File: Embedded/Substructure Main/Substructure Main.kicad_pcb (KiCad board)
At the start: 2 copper layers, 60 parts, among them J1 MicroSD, J2 C Pins, J3 Coin Cell, U1 G0 FFC, U10 LD1117S50TR_SOT223, U2 G1 FFC, U3 S FFC, U4 USB2513B_Bi, U5 MCP7940N-xMNY, U6 INA220AIDGSR, U7 M FFC, U8 F FFC, U9 LD1117S33TR_SOT223, Y1 TSX-3225 24MF18X-C0, Y2 CM7V-T1A

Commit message: Begun Component Layout
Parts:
- U7: moved to B.Cu
- moved U1 98.5 mm to (106.0, 84.2), turned to -90 degrees
- moved U2 96.5 mm to (144.7, 83.0), turned to 90 degrees
- moved U3 93.8 mm to (144.8, 93.2), turned to 90 degrees
- moved C12 93.1 mm to (137.5, 131.7)
- moved C15 93.1 mm to (137.5, 129.0)
- moved C10 93.1 mm to (142.7, 137.0)
- moved C11 93.1 mm to (142.7, 138.0)
- moved C13 93.1 mm to (140.5, 136.0)
- moved C16 93.1 mm to (143.5, 136.0)
- moved C22 93.1 mm to (147.0, 132.2)
- moved C4 93.1 mm to (138.2, 124.4)
- moved C5 93.1 mm to (144.9, 124.4)
- moved C6 93.1 mm to (137.5, 126.0)
- moved C7 93.1 mm to (147.0, 131.2)
- moved C8 93.1 mm to (137.5, 127.0)
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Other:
- board outline added: 50 x 40 mm

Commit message: Added Sensored V2 Board
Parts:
- U11: value ~ -> Sensored; footprint Sensored:Sensored -> Custom Modules:Sensored
- moved U11 28.0 mm to (93.4, 139.8)
- renumbered C26 to C1, C3 to C10, C4 to C11, C5 to C12, C6 to C13, C7 to C14, C8 to C15, C9 to C16, C10 to C17, C11 to C18, C12 to C19, C28 to C2, C13 to C20, C14 to C21, C15 to C22, C16 to C23, C22 to C24, C17 to C25, C18 to C26, C19 to C27, C20 to C28, C21 to C29, C27 to C3, C29 to C4, C25 to C5, C1 to C6, C23 to C7, C2 to C8, C24 to C9, J2 to J1, J1 to J2, R3 to R1, R4 to R2, R1 to R3, R2 to R4, U6 to U10, U8 to U2, U7 to U4, U2 to U5, U9 to U6, U10 to U7, U4 to U8, U5 to U9

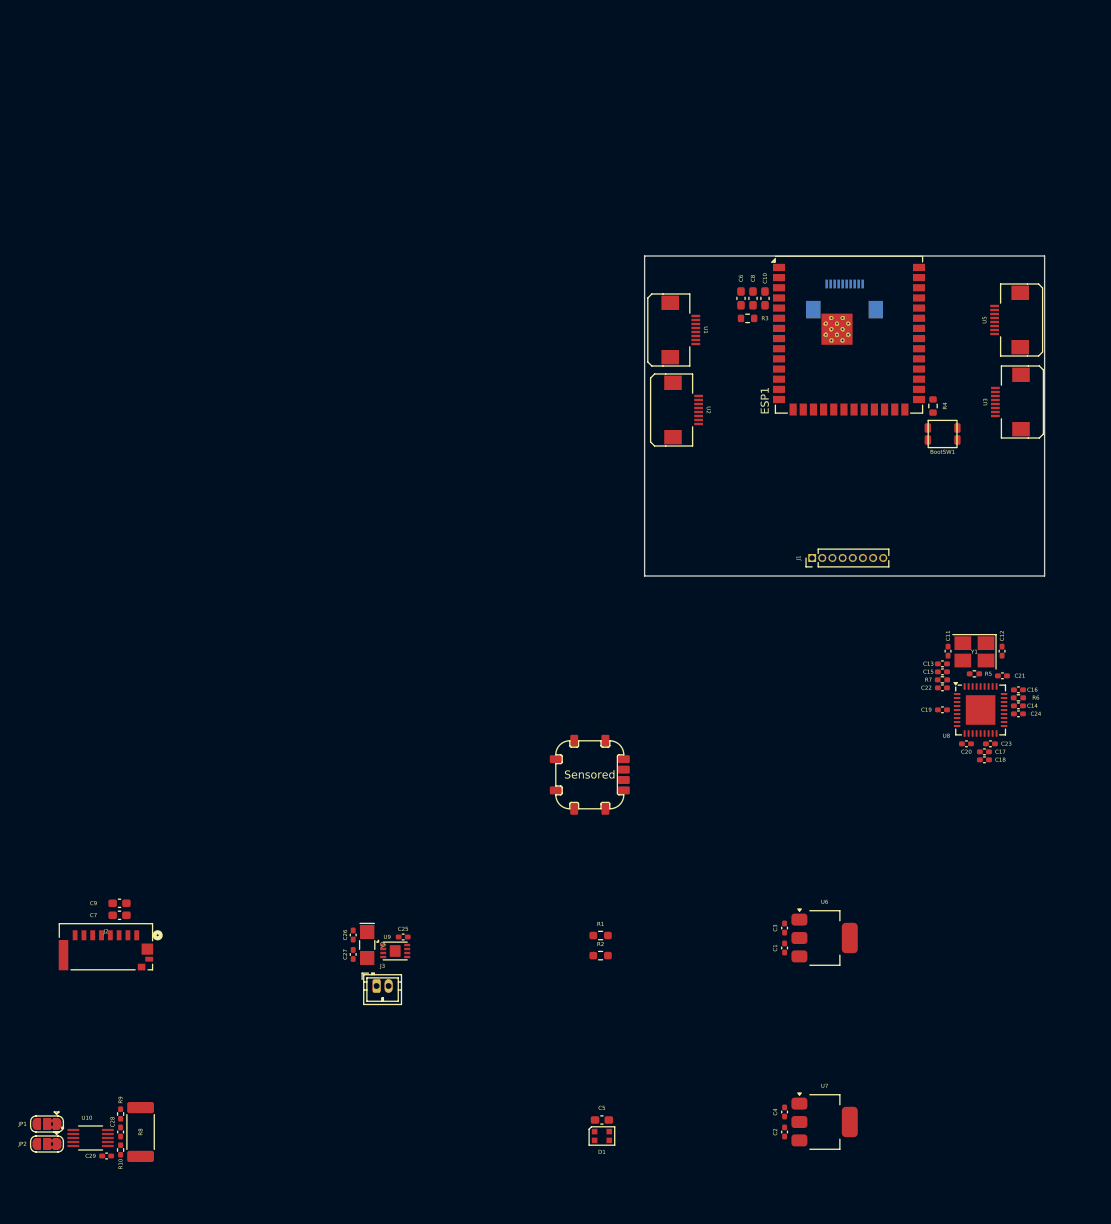
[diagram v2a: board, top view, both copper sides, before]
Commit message: Added Component placement & edge cuts
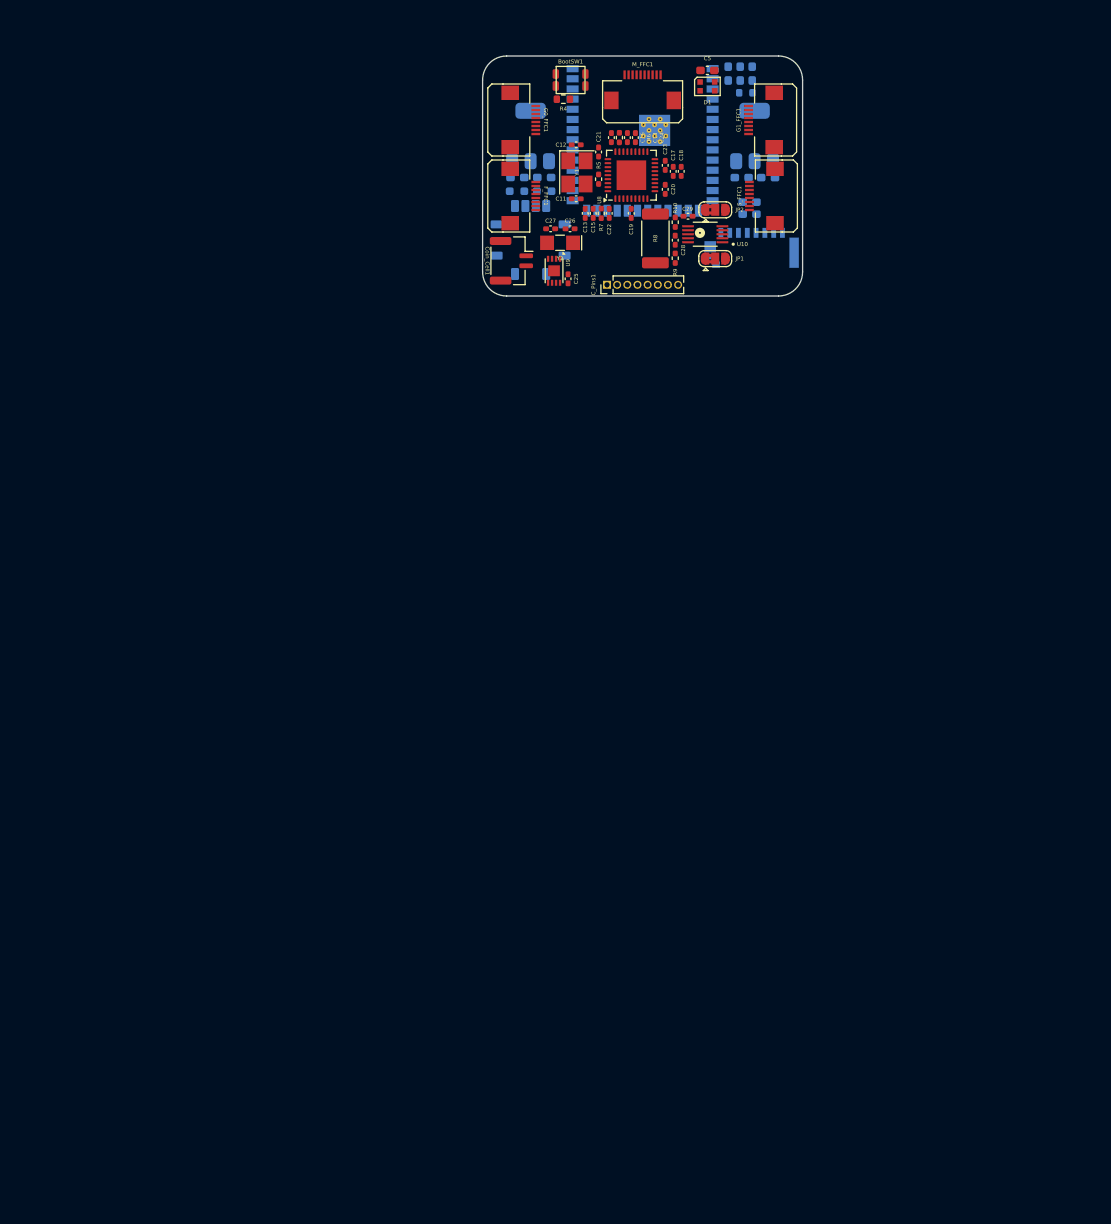
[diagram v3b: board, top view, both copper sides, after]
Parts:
- C1, C2, C3, C4: footprint Capacitor_SMD:C_0402_1005Metric_Pad0.74x0.62mm_HandSolder -> Capacitor_SMD:C_0603_1608Metric_Pad1.08x0.95mm_HandSolder; moved to B.Cu
- C10, C6, C7, C8, C9, ESP1, J2, R1, R2, R3, U11, U6, U7: moved to B.Cu
- Coin_Cell1: renamed from J3; footprint Connector_JST:JST_ZH_B2B-ZR_1x02_P1.50mm_Vertical -> Connector_JST:JST_GH_SM02B-GHS-TB_1x02-1MP_P1.25mm_Horizontal
- M_FFC1: renamed from U4; moved to F.Cu
- moved JP2 143.6 mm to (109.1, 69.2), turned to 0 degrees
- moved C29 138.1 mm to (105.7, 70.0), turned to 0 degrees
- moved JP1 136.7 mm to (109.1, 75.3), turned to 0 degrees
- moved U10 136.6 mm to (107.8, 72.3), turned to 180 degrees
- moved R10 135.1 mm to (104.1, 70.8), turned to -90 degrees
- moved C5 131.9 mm to (108.1, 51.8)
- moved D1 131.9 mm to (108.1, 53.8)
- moved C28 131.3 mm to (104.1, 73.0), turned to 90 degrees
- moved R8 128.9 mm to (101.6, 72.8), turned to 90 degrees
- moved U7 128.6 mm to (86.0, 60.0), turned to 90 degrees
- moved R9 127.5 mm to (104.1, 75.3), turned to 90 degrees
- moved C2 123.9 mm to (84.3, 65.2), turned to 0 degrees
- moved C4 120.6 mm to (87.7, 65.2), turned to 0 degrees
- moved J2 119.3 mm to (113.6, 72.1), turned to 180 degrees
- moved C7 119.0 mm to (113.4, 68.3)
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- renumbered J1 to C_Pins1, U2 to F_FFC1, U1 to G0_FFC1, U5 to G1_FFC1, U3 to S_FFC1
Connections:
- Coin_Cell1 pad 1: Net-(J3-Pin_1) -> GND
- Coin_Cell1 pad 2: GND -> Net-(Coin_Cell1-Pin_2)
- U9 pad 3: Net-(J3-Pin_1) -> Net-(Coin_Cell1-Pin_2)
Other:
- board size 50 x 40 mm -> 40 x 30 mm

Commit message: Modified Files (Synchronisation Update)
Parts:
- moved C5 3.20 mm to (108.0, 55.0)
- moved C6 3.10 mm to (110.6, 52.1)
- moved R3 1.50 mm to (111.4, 54.5), turned to 180 degrees
- moved C10 1.40 mm to (112.1, 52.1)
- moved C8 1.40 mm to (113.6, 52.1)
- moved D1 0.81 mm to (108.0, 53.0)
- moved ESP1 0.09 mm to (100.0, 59.9)
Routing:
- net +3V3: track 0.00 -> 13.0 mm
- net Net-(U8-XTALOUT): track 0.00 -> 8.09 mm
- net Net-(U8-XTALIN/CLKIN): track 0.00 -> 5.14 mm
- net Net-(ESP1-GPIO0/BOOT): track 0.00 -> 3.96 mm
- net Net-(ESP1-EN): track 0.00 -> 3.61 mm
- net Net-(U8-CRFILT): track 0.00 -> 3.33 mm
- net I2C SDA: track 0.00 -> 1.91 mm
- net I2C SCL: track 0.00 -> 1.91 mm
- added copper zone on F.Cu, net +3V3
- added copper zone on B.Cu, net GND

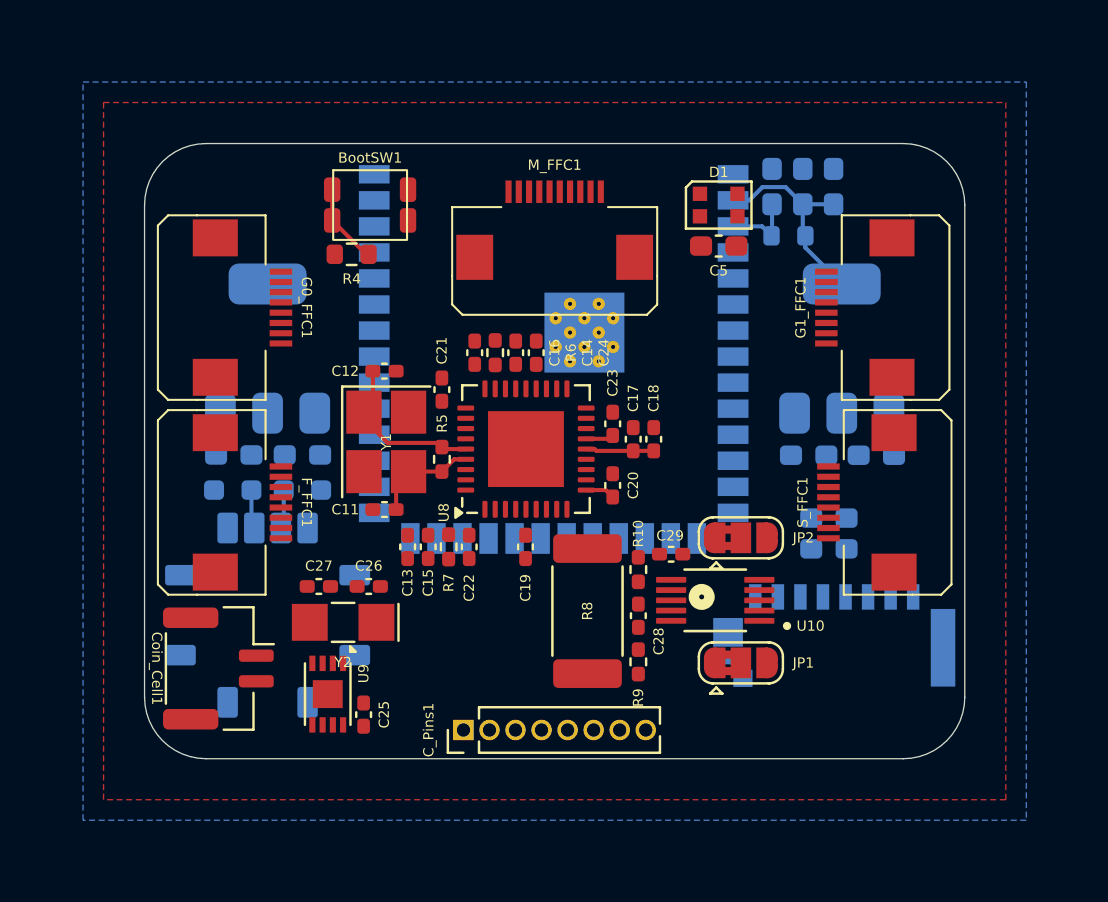
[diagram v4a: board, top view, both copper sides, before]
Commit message: Modified Board from 2 Layer to 4 Layers & Routed close components
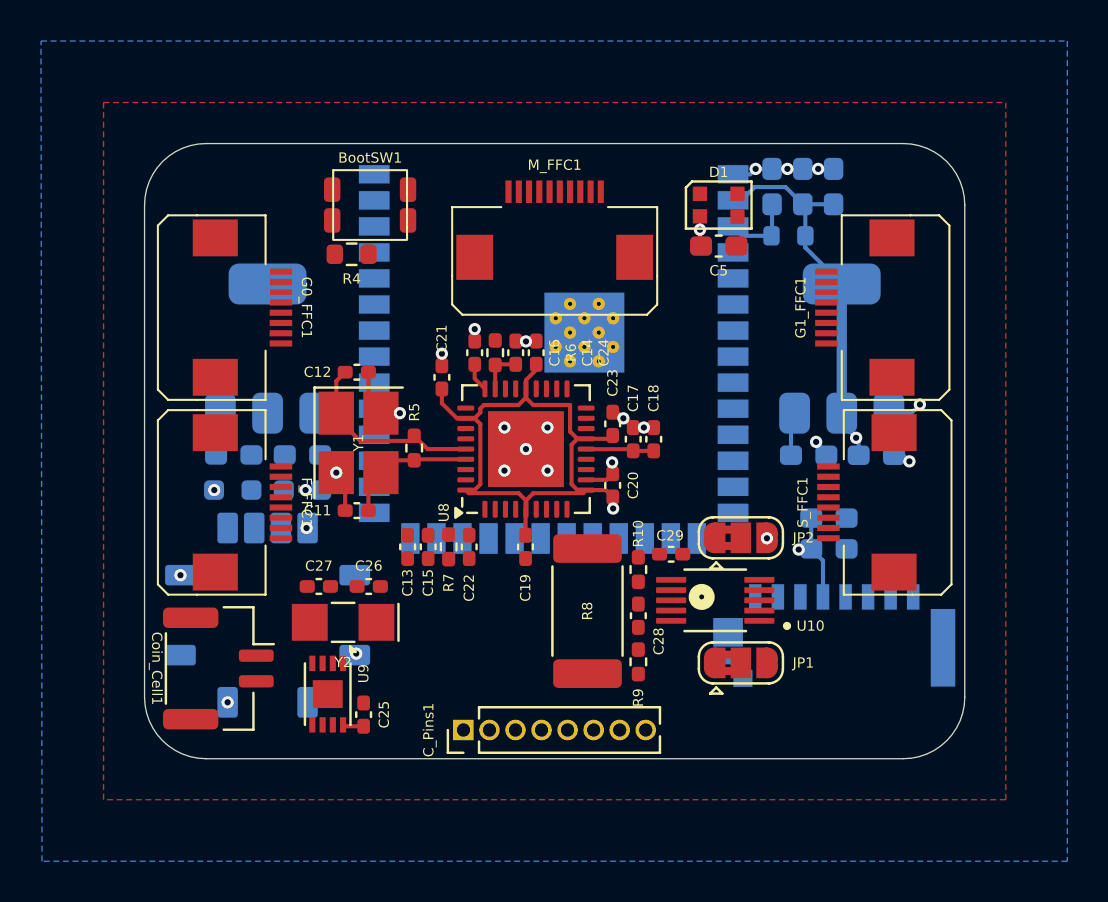
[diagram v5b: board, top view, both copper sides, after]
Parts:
- moved R5 1.46 mm to (93.2, 64.8)
- moved C11 1.35 mm to (90.3, 67.9)
- moved C12 1.35 mm to (90.3, 61.1)
- moved Y1 1.35 mm to (90.4, 64.6)
- moved C21 0.60 mm to (94.5, 61.4)
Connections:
- U8 pad 1: Main USB - -> Snoot USB -
- U8 pad 2: Main USB + -> HUD USB +
- U8 pad 6: Snoot USB - -> Main USB -
- U8 pad 7: HUD USB + -> Main USB +
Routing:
- net +3V3: track 13.0 -> 56.7 mm, vias 0 -> 10
- net GND: track 0.00 -> 29.1 mm, vias 0 -> 20
- net Net-(ESP1-GPIO0/BOOT): track 3.96 -> 0.00 mm
- net Net-(U8-RESET_N): track 0.00 -> 2.18 mm
- net +5VS: track 0.00 -> 2.12 mm
- net I2C SDA: track 1.91 -> 0.00 mm
- net I2C SCL: track 1.91 -> 0.00 mm
- net Net-(U8-XTALOUT): track 8.09 -> 9.53 mm
- net +5VP: track 0.00 -> 1.40 mm
- net Net-(U8-XTALIN/CLKIN): track 5.14 -> 6.51 mm
- added copper zone on In2.Cu, net +3V3
- added copper zone on In1.Cu, net GND
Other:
- copper layers 2 -> 4

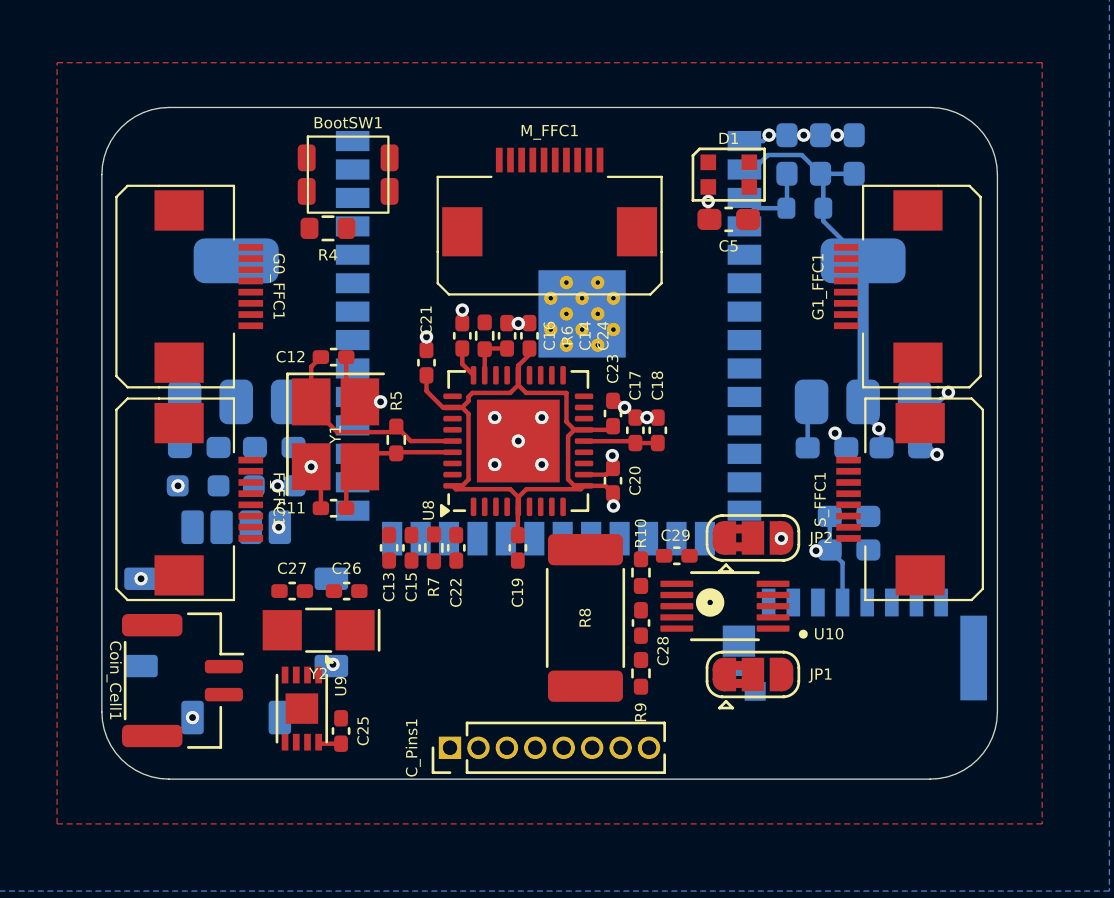
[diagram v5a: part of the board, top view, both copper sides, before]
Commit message: Added Routing for USB lanes, power & other data lanes
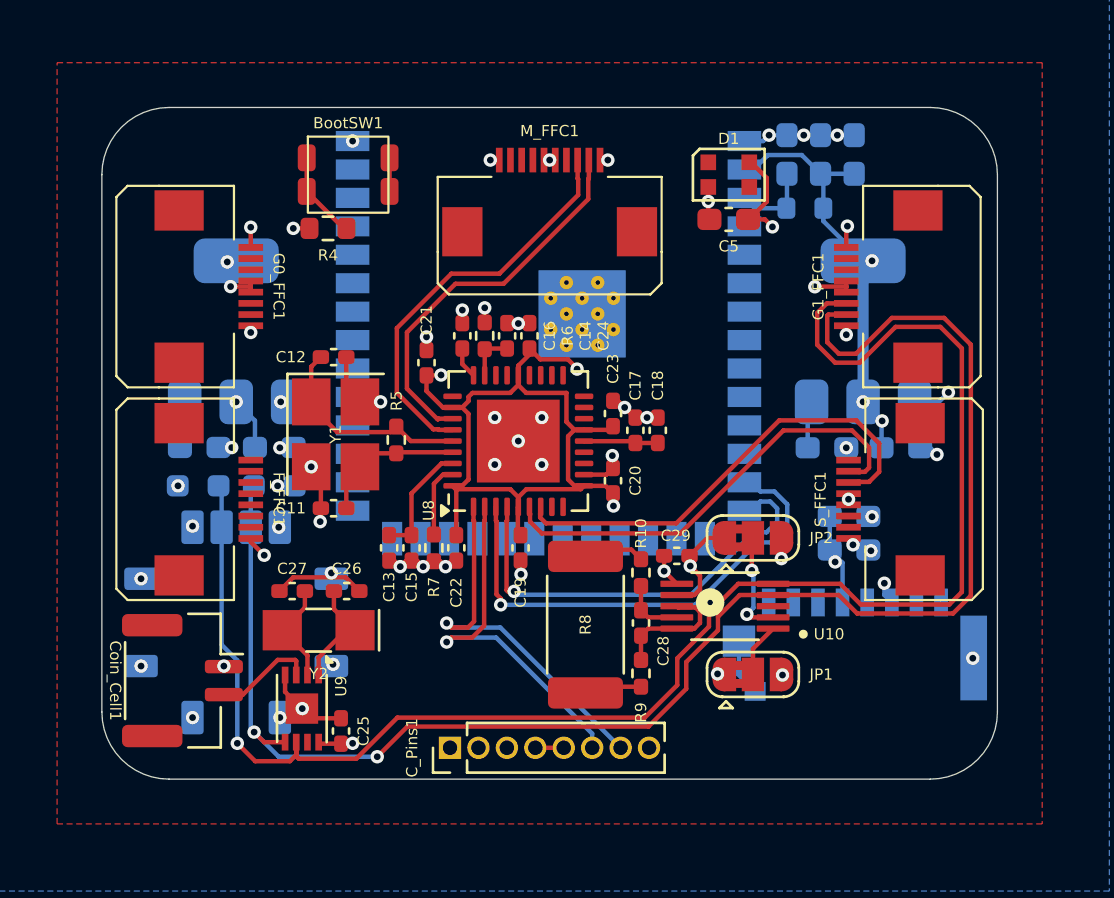
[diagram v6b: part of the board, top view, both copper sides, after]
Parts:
- moved R8 0.30 mm to (101.6, 73.1)
- moved C19 0.12 mm to (98.7, 69.7)
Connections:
- U8 pad 1: Snoot USB - -> HUD USB -
- U8 pad 3: HUD USB - -> Main USB -
- U8 pad 4: Snoot USB + -> Main USB +
- U8 pad 6: Main USB - -> Snoot USB -
- U8 pad 7: Main USB + -> Snoot USB +
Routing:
- net I2C SCL: track 0.00 -> 72.4 mm, vias 0 -> 1
- net I2C SDA: track 0.00 -> 70.9 mm, vias 0 -> 2
- net GND: track 29.1 -> 59.0 mm, vias 20 -> 49
- net Main USB -: track 0.00 -> 22.0 mm, vias 0 -> 1
- net Snoot USB +: track 0.00 -> 20.9 mm
- net Snoot USB -: track 0.00 -> 20.2 mm
- net Main USB +: track 0.00 -> 19.6 mm, vias 0 -> 1
- net Power USB +: track 0.00 -> 18.2 mm
- net Power USB -: track 0.00 -> 17.4 mm
- net HUD USB -: track 0.00 -> 16.6 mm, vias 0 -> 1
- net HUD USB +: track 0.00 -> 16.3 mm, vias 0 -> 1
- net +5V: track 0.00 -> 12.7 mm, vias 0 -> 6
- net +3V3: track 56.7 -> 67.2 mm, vias 10 -> 19
- net Net-(U10-VBUS): track 0.00 -> 5.59 mm
- net Net-(U8-PLLFILT): track 0.00 -> 5.25 mm
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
